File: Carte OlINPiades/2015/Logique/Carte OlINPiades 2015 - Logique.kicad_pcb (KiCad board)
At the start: 2 copper layers, 29 parts, among them U1 dsPIC33FJ128MC802, U2 7805, U3 LM2937-3.3

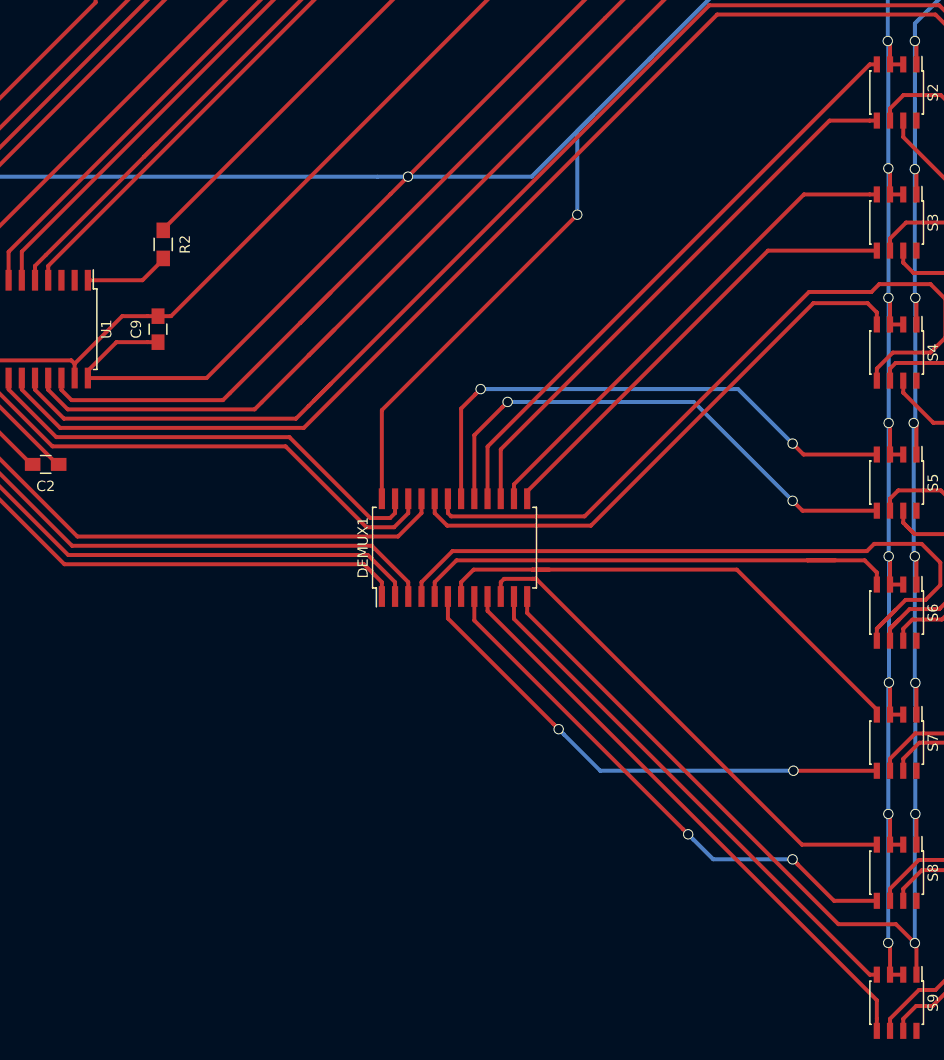
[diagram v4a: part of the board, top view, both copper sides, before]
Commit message: rapproche le démux des pins headers
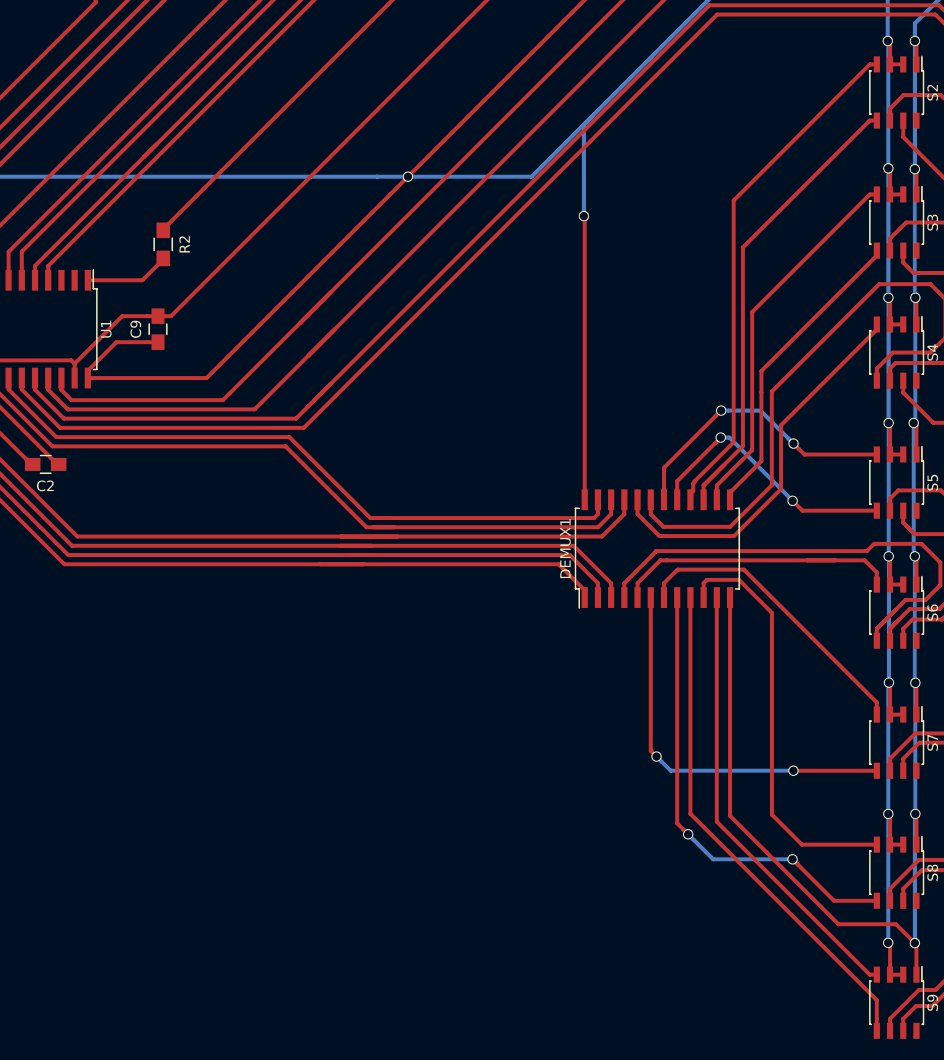
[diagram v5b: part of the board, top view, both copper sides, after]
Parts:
- moved DEMUX1 19.5 mm to (182.0, 100.1)
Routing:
- net RB9: track 55.5 -> 80.4 mm
- net Net-(DEMUX1-Pad17): track 50.5 -> 25.7 mm
- net Net-(DEMUX1-Pad18): track 52.1 -> 28.3 mm
- net RB6: track 56.4 -> 79.7 mm
- net RB8: track 56.4 -> 79.0 mm
- net RB10: track 48.2 -> 69.6 mm
- net RB7: track 56.4 -> 77.6 mm
- net RB11: track 44.9 -> 66.1 mm
- net Net-(DEMUX1-Pad7): track 49.5 -> 28.8 mm
- net Net-(DEMUX1-Pad5): track 49.0 -> 29.6 mm
- net Net-(DEMUX1-Pad4): track 67.2 -> 47.8 mm
- net Net-(DEMUX1-Pad20): track 54.8 -> 37.6 mm
- net Net-(DEMUX1-Pad13): track 43.9 -> 29.8 mm
- net Net-(DEMUX1-Pad19): track 71.9 -> 58.4 mm
- net Net-(DEMUX1-Pad6): track 49.4 -> 37.3 mm
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
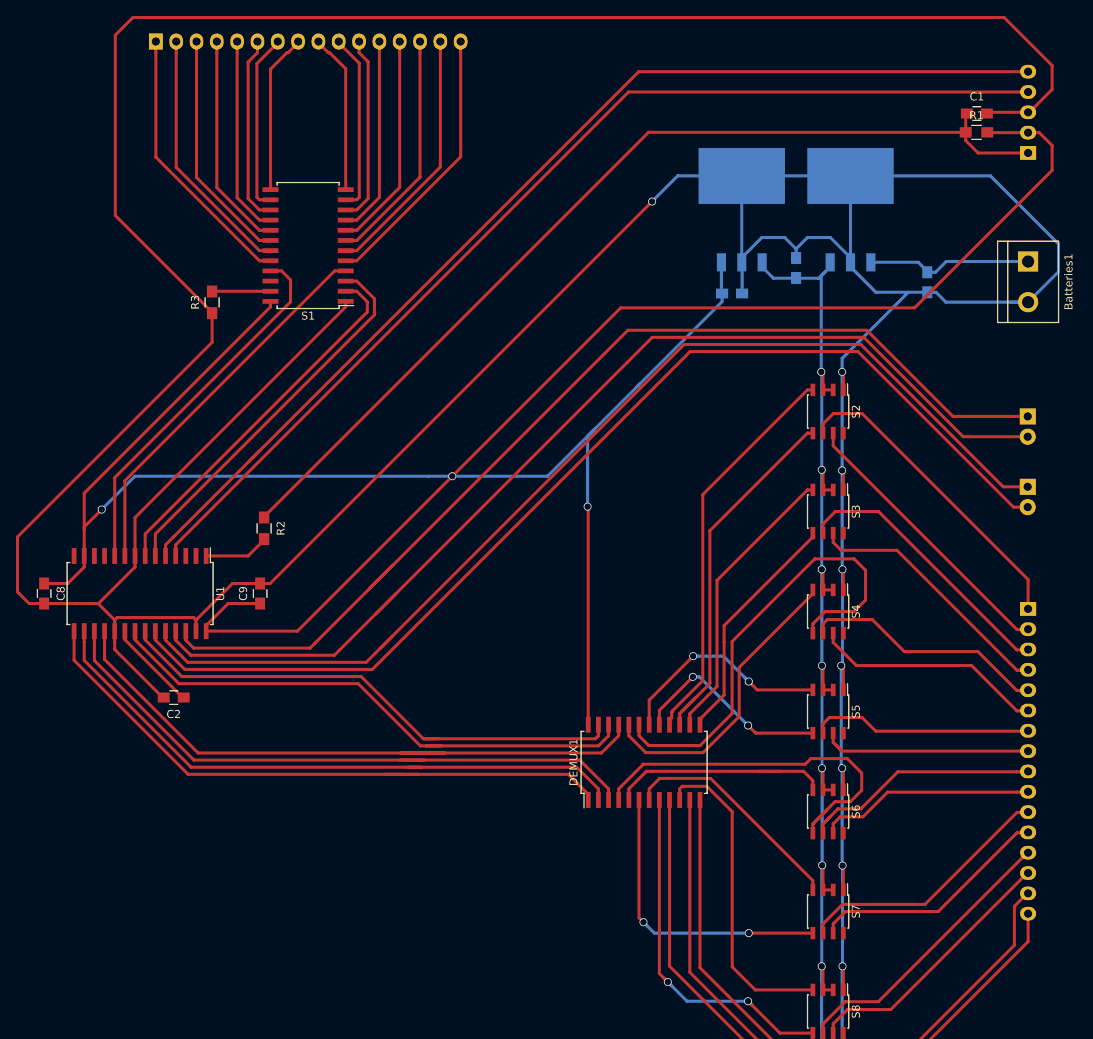
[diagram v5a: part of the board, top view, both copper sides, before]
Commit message: rapproche le dsPIC
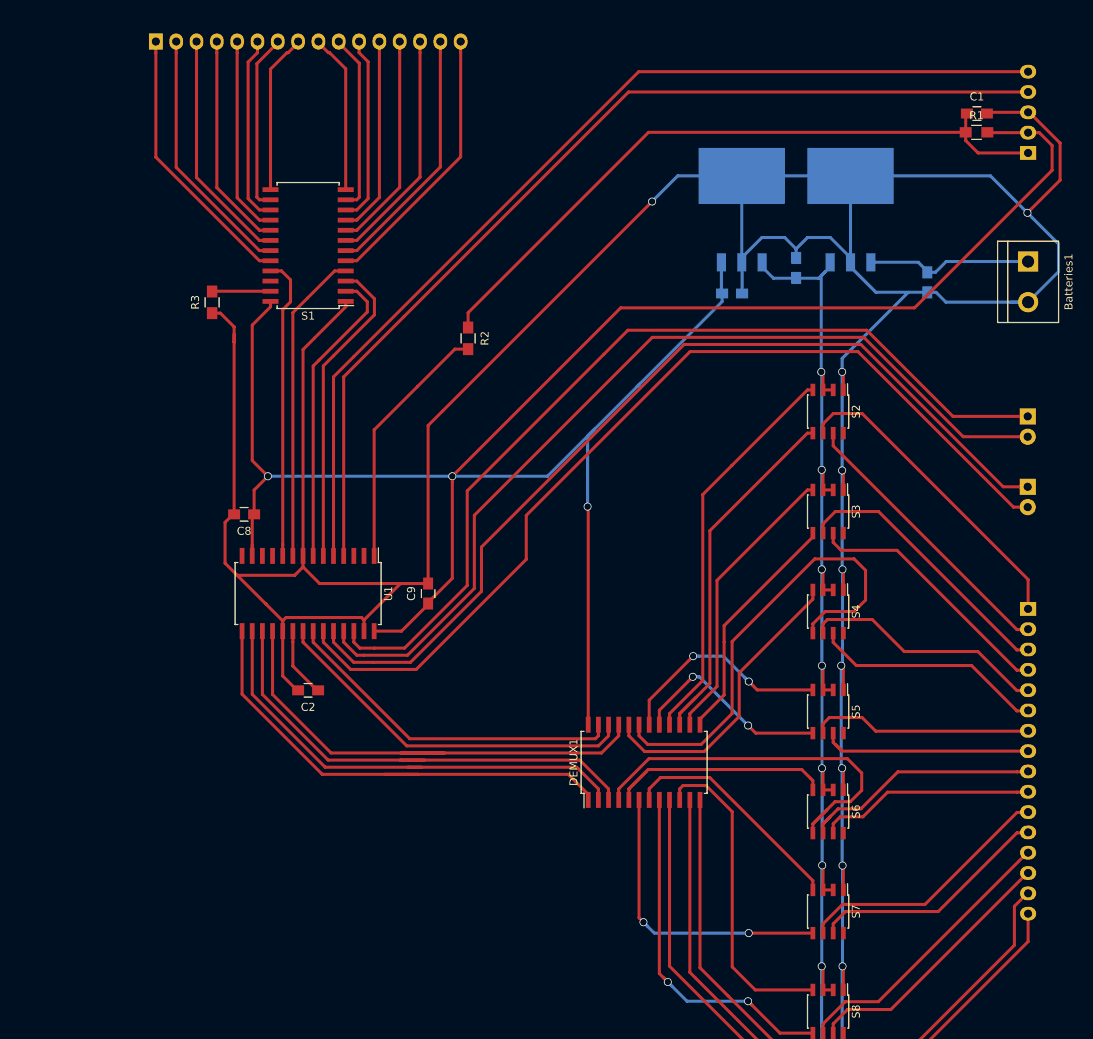
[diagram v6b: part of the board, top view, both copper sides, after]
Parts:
- moved R2 34.8 mm to (160.0, 47.1)
- moved C8 26.9 mm to (132.0, 69.1), turned to 180 degrees
- moved C9 21.0 mm to (155.0, 79.0)
- moved U1 21.0 mm to (140.0, 79.0)
- moved C2 16.8 mm to (140.0, 91.1)
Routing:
- net GND: track 692.0 -> 522.2 mm, vias 9 -> 10
- net +3.3V: track 333.1 -> 272.4 mm
- net Net-(C1-Pad1): track 119.7 -> 85.3 mm
- net Net-(R2-Pad2): track 8.17 -> 31.7 mm
- net RB10: track 69.6 -> 46.8 mm
- net RB11: track 66.1 -> 43.6 mm
- net RB13: track 136.1 -> 116.3 mm
- net RB14: track 133.6 -> 114.5 mm
- net RB8: track 79.0 -> 60.5 mm
- net RB6: track 79.7 -> 61.2 mm
- net RB7: track 77.6 -> 59.1 mm
- net RB9: track 80.4 -> 62.0 mm
- net RB15: track 131.9 -> 113.8 mm
- net RB12: track 136.2 -> 118.6 mm
- net PGC: track 135.5 -> 125.0 mm
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
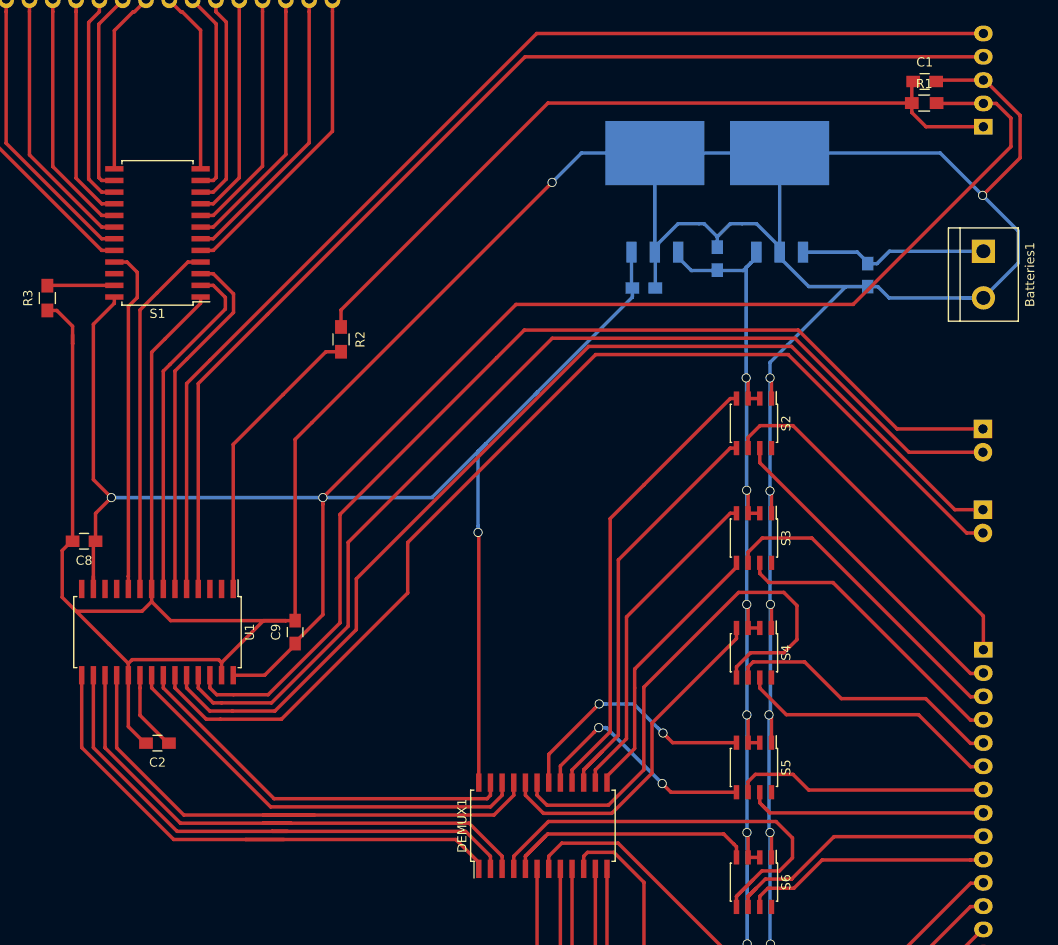
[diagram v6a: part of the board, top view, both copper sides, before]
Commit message: nettoyage de pistes
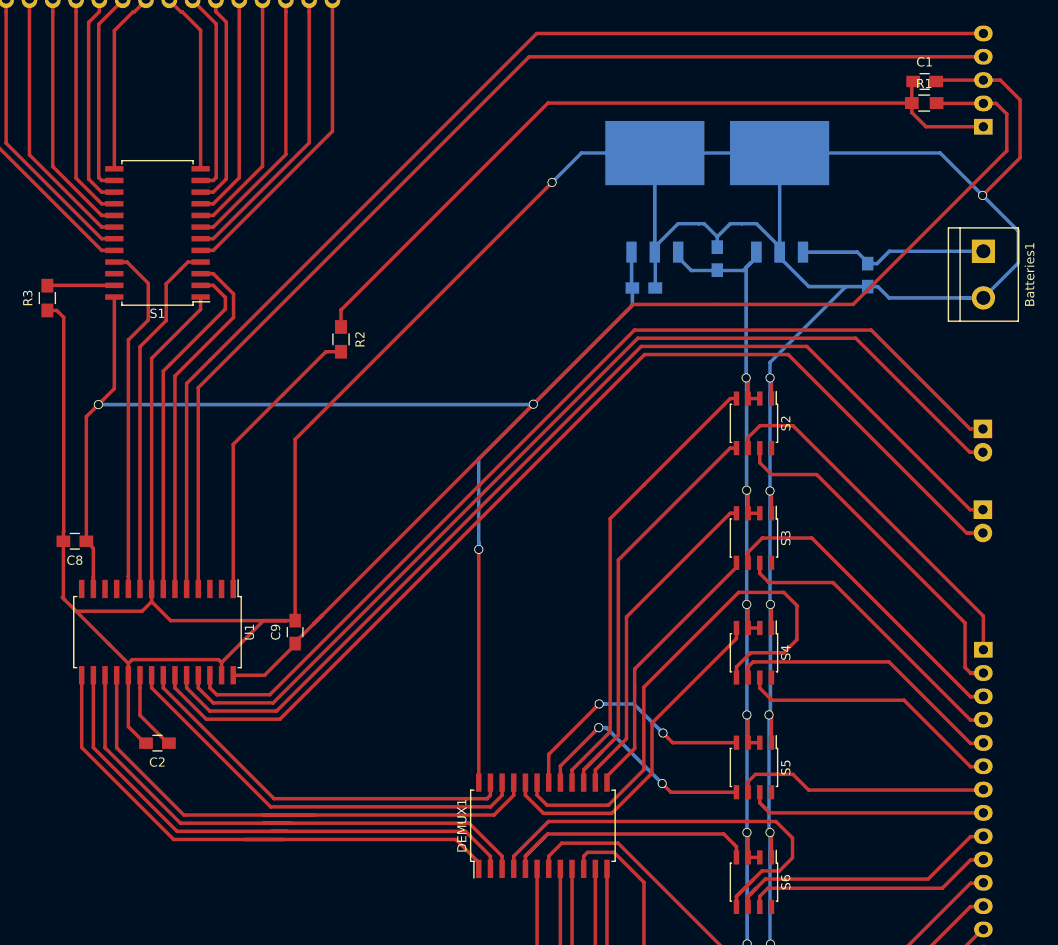
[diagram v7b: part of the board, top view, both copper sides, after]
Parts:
- moved C8 1.00 mm to (131.0, 69.1)
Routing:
- net RB15: track 113.8 -> 106.8 mm
- net RB14: track 114.5 -> 109.2 mm
- net Net-(H2-Pad2): track 35.5 -> 39.7 mm
- net RB13: track 116.3 -> 113.0 mm
- net RB12: track 118.6 -> 115.4 mm
- net +3.3V: track 272.4 -> 269.4 mm
- net RA3: track 37.9 -> 38.9 mm
- net GND: track 522.2 -> 521.6 mm

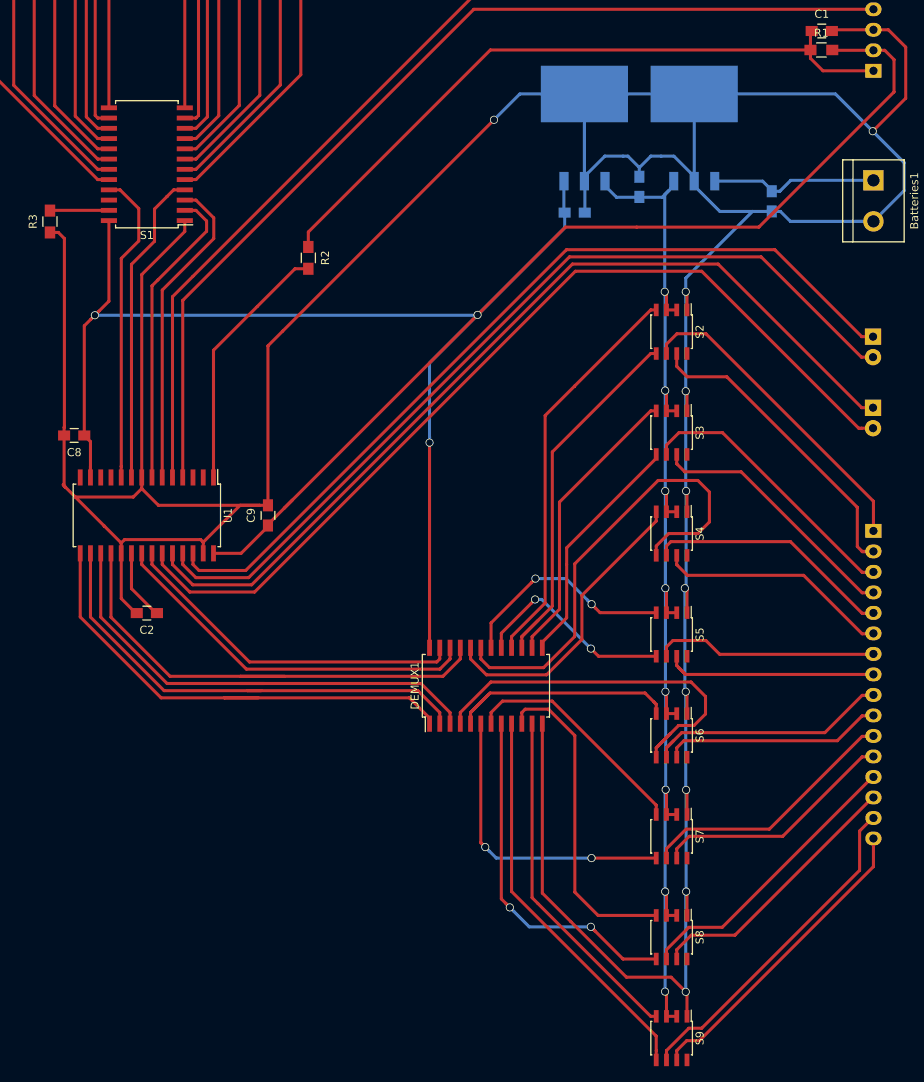
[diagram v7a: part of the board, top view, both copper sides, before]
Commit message: nettoyage et changement de taille de certaines pistes
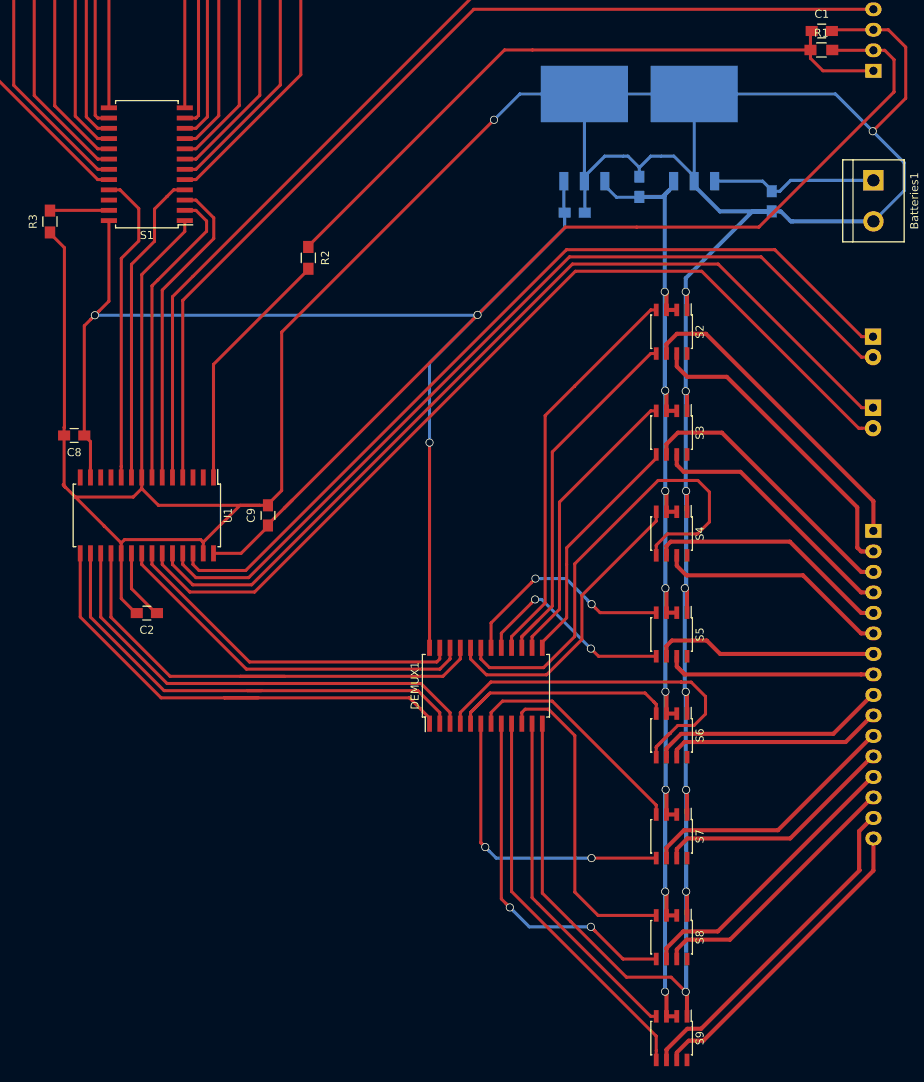
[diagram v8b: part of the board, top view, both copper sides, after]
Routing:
- net +5V: track 143.3 -> 155.9 mm
- net Net-(H2-Pad15): track 41.6 -> 49.0 mm
- net Net-(H2-Pad1): track 39.6 -> 43.3 mm
- net Net-(H2-Pad8): track 27.1 -> 29.9 mm
- net GND: track 521.6 -> 523.4 mm
- net Net-(H2-Pad9): track 30.7 -> 29.5 mm
- net Net-(C1-Pad1): track 85.3 -> 84.3 mm
- net Net-(R2-Pad2): track 31.7 -> 30.7 mm
